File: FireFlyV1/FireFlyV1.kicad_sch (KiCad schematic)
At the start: 28 parts, among them SW1 PTS810SJG250SMTRLFS, U1 RP2040, U2 W25Q32JVSS, U3 ABM8-272-T3_C20625731, U4 NCP1117ST33T3G, U5 MCP6001T-I/OT

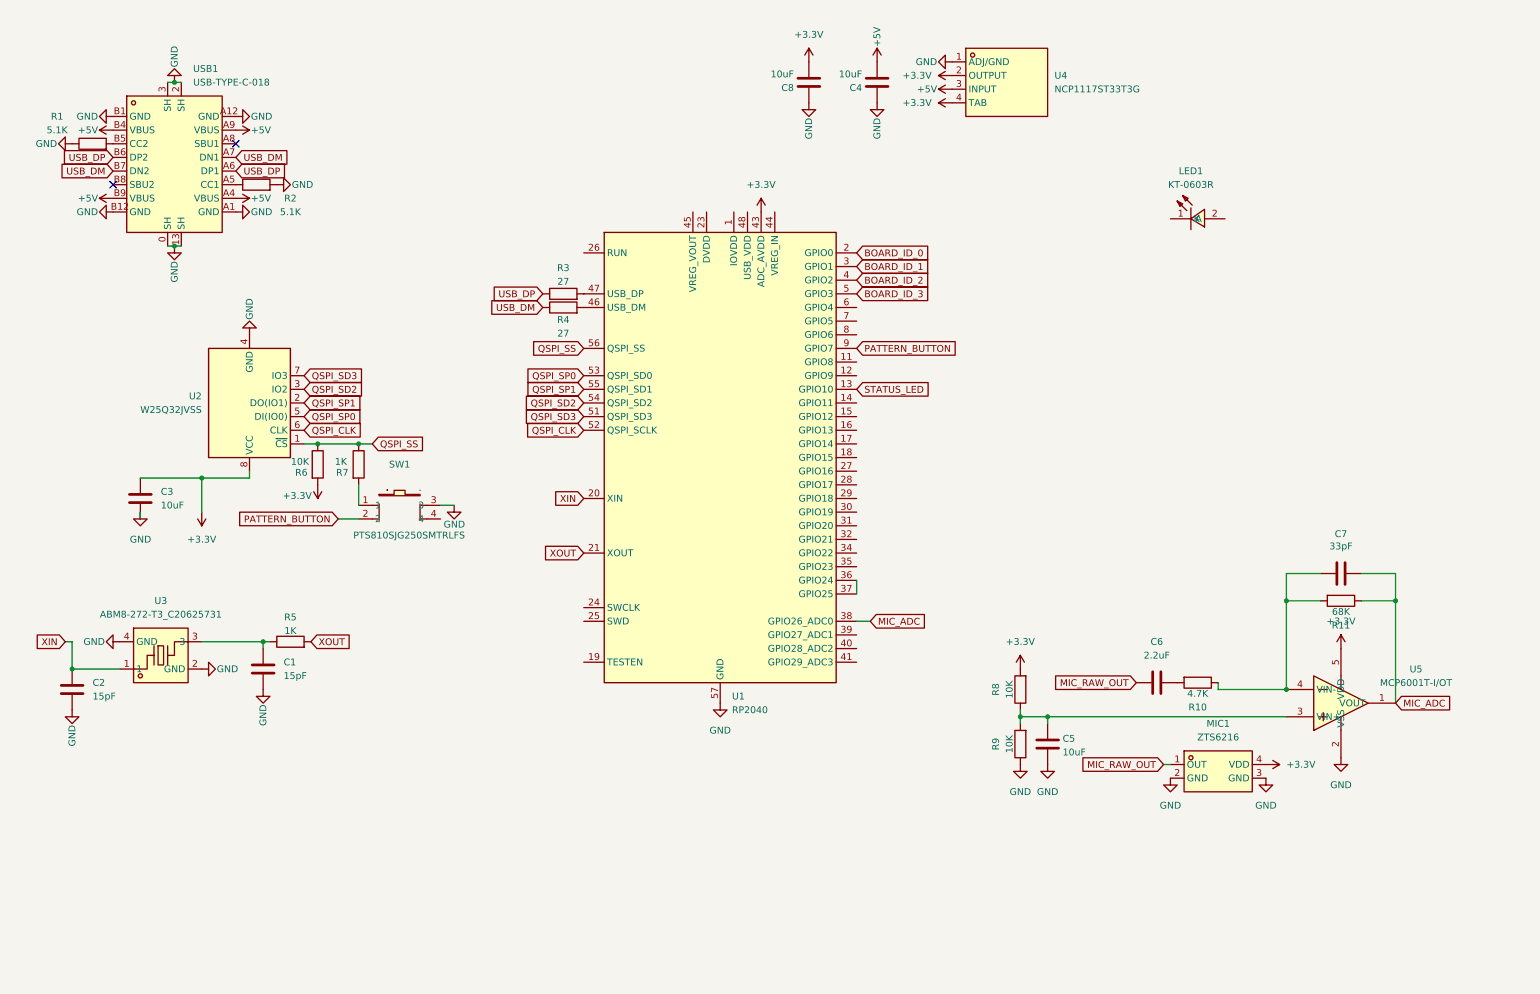
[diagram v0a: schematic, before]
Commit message: finished first draft of schematic
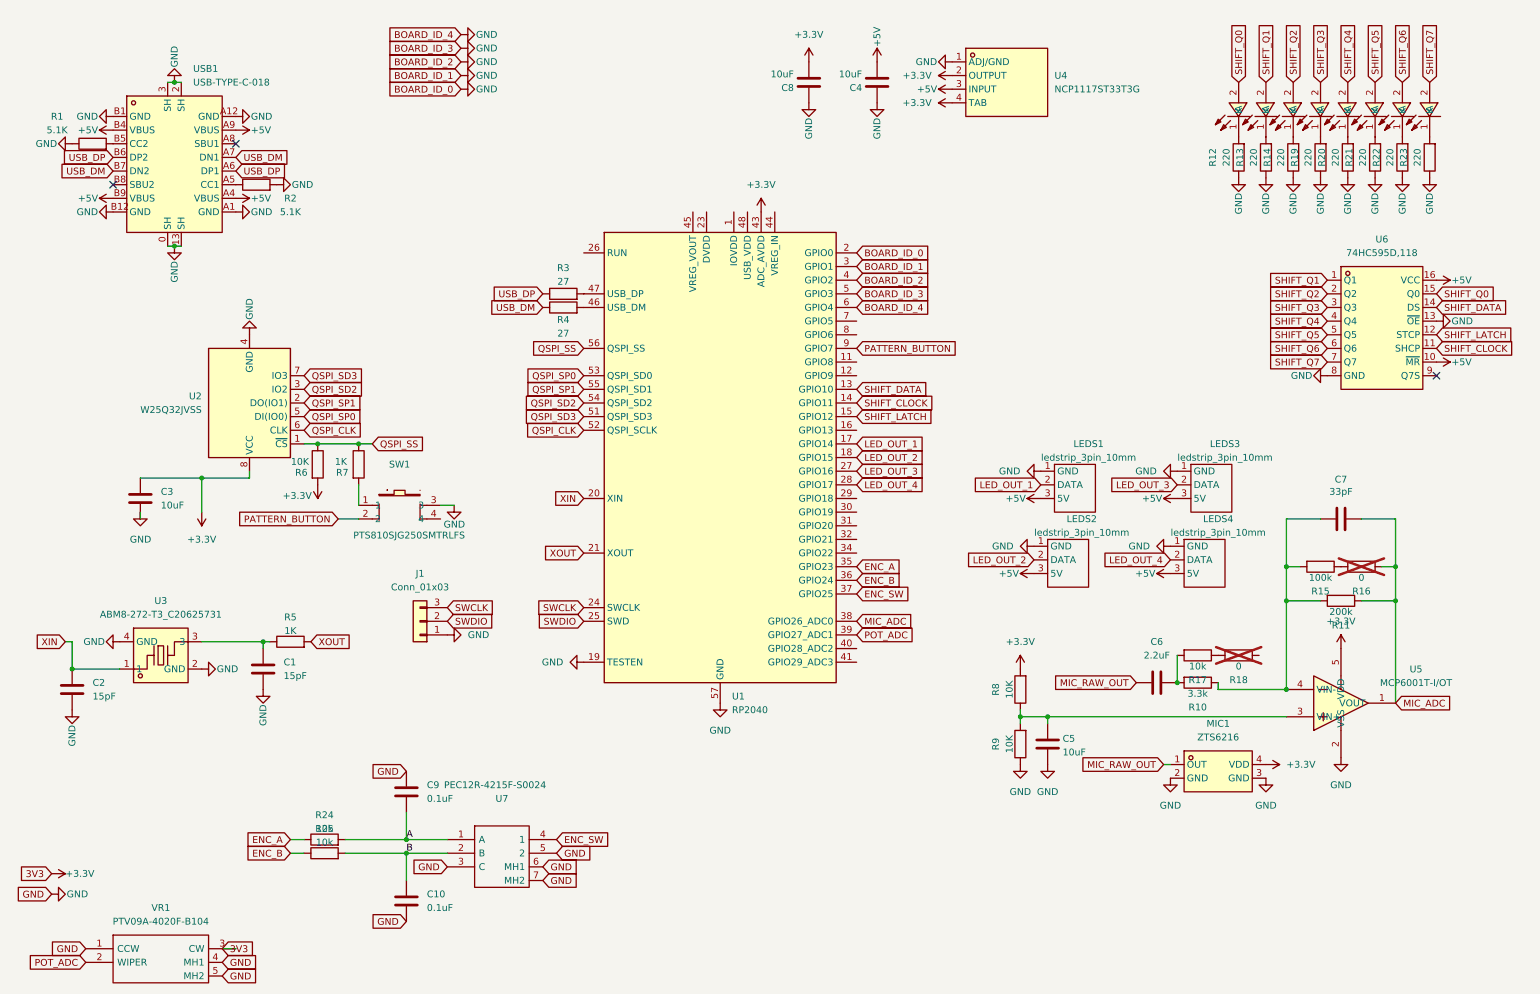
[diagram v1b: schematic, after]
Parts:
- added C10, C9: 0.1uF, symbol Device:C
- added J1: Conn_01x03, symbol Connector_Generic:Conn_01x03
- added LED2, LED3, LED4, LED5, LED6, LED7, LED8: KT-0603R, easyeda2kicad:LED0603-RD, symbol easyeda2kicad:KT-0603R
- added LEDS1, LEDS2, LEDS3, LEDS4: ledstrip_3pin_10mm, kylarLEDs:ledstrip_3pin_10mm, symbol kylarLEDs:ledstrip_3pin_10mm
- added R12, R13, R14, R19, R20, R21, R22, R23: 220, Resistor_SMD:R_0402_1005Metric, symbol Device:R
- added R15: 100k, Resistor_SMD:R_0402_1005Metric, symbol Device:R
- added R16, R18: 0, Resistor_SMD:R_0402_1005Metric, symbol Device:R
- added R17, R24, R25: 10k, Resistor_SMD:R_0402_1005Metric, symbol Device:R
- added U6: 74HC595D,118, easyeda2kicad:SOIC-16_L9.9-W3.9-P1.27-LS6.0-BL, symbol easyeda2kicad:74HC595D,118
- added U7: PEC12R-4215F-S0024, SamacSys_Parts:PEC12R-4XXXF-SXXXX_court, symbol SamacSys_Parts:PEC12R-4215F-S0024
- added VR1: PTV09A-4020F-B104, SamacSys_Parts:PTV09A4020FB103, symbol SamacSys_Parts:PTV09A-4020F-B104
- R1, R2, R3, R4, R5, R6, R7, R8, R9: footprint (none) -> Resistor_SMD:R_0402_1005Metric
- R10: value 4.7K -> 3.3k; footprint (none) -> Resistor_SMD:R_0402_1005Metric
- R11: value 68K -> 200k; footprint (none) -> Resistor_SMD:R_0402_1005Metric
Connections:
- net BOARD_ID_0 is gone; now on net GND: U1.2 (GPIO0)
- net BOARD_ID_1 is gone; now on net GND: U1.3 (GPIO1)
- net BOARD_ID_2 is gone; now on net GND: U1.4 (GPIO2)
- net BOARD_ID_3 is gone; now on net GND: U1.5 (GPIO3)
- net +3.3V: now also VR1.3 (CW)
- net +5V: now also LEDS1.3 (5V), LEDS2.3 (5V), LEDS3.3 (5V), LEDS4.3 (5V), U6.10 (~{MR}), U6.16 (VCC)
- net GND: now also U1.19 (TESTEN), U1.6 (GPIO4), C10.1, C9.2, J1.1 (Pin_1), LEDS1.1 (GND), LEDS2.1 (GND), LEDS3.1 (GND), LEDS4.1 (GND), R12.1, R13.1, R14.1, R19.1, R20.1, R21.1, R22.1, R23.1, U6.13 (~{OE}), U6.8 (GND), U7.3 (C), U7.5 (2), U7.6 (MH1), U7.7 (MH2), VR1.1 (CCW), VR1.4 (MH1), VR1.5 (MH2)
- net MIC_ADC: now also R16.1
- net SHIFT_CLOCK: now reaches U1.14 (GPIO11)
- net SHIFT_CLOCK: now also U6.11 (SHCP)
- net SHIFT_LATCH: now reaches U1.15 (GPIO12)
- net SHIFT_LATCH: now also U6.12 (STCP)
- net LED_OUT_1: now reaches U1.17 (GPIO14)
- net LED_OUT_1: now also LEDS1.2 (DATA)
- net LED_OUT_2: now reaches U1.18 (GPIO15)
- net LED_OUT_2: now also LEDS2.2 (DATA)
- net SWCLK: now reaches U1.24 (SWCLK)
- net SWCLK: now also J1.3 (Pin_3)
- net SWDIO: now reaches U1.25 (SWD)
- net SWDIO: now also J1.2 (Pin_2)
- net LED_OUT_3: now reaches U1.27 (GPIO16)
- net LED_OUT_3: now also LEDS3.2 (DATA)
- net LED_OUT_4: now reaches U1.28 (GPIO17)
- net LED_OUT_4: now also LEDS4.2 (DATA)
- net ENC_A: now reaches U1.35 (GPIO23)
- net ENC_A: now also R24.1
- net ENC_B: now reaches U1.36 (GPIO24)
- net ENC_B: now also R25.1; no longer U1.37 (GPIO25)
- net POT_ADC: now reaches U1.39 (GPIO27_ADC1)
- net POT_ADC: now also VR1.2 (WIPER)
- net at LED1.1 (K): now also R12.2
- net SHIFT_Q0: now reaches LED1.2 (A)
- net SHIFT_Q0: now also U6.15 (Q0)
- net at C7.1, R10.1, R11.2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: now also R15.2
- net at C6.2, R10.2: now also R17.2
- net STATUS_LED renamed SHIFT_DATA
- net SHIFT_DATA: now also U6.14 (DS)
- new net: LED2.1 (K), R13.2
- new net: LED8.1 (K), R23.2
- new net: R17.1, R18.2
- new net: R15.1, R16.2
- new net: LED6.1 (K), R21.2
- new net: LED3.1 (K), R14.2
- new net: LED4.1 (K), R19.2
- new net: LED5.1 (K), R20.2
- new net: LED7.1 (K), R22.2
- new net A: C9.1, R24.2, U7.1 (A)
- new net B: C10.2, R25.2, U7.2 (B)
- new net ENC_SW: U1.37 (GPIO25), U7.4 (1)
- new net SHIFT_Q1: LED2.2 (A), U6.1 (Q1)
- new net SHIFT_Q2: LED3.2 (A), U6.2 (Q2)
- new net SHIFT_Q3: LED4.2 (A), U6.3 (Q3)
- new net SHIFT_Q4: LED5.2 (A), U6.4 (Q4)
- new net SHIFT_Q5: LED6.2 (A), U6.5 (Q5)
- new net SHIFT_Q6: LED7.2 (A), U6.6 (Q6)
- new net SHIFT_Q7: LED8.2 (A), U6.7 (Q7)
- no-connect marks 2 -> 3
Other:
- moved on the sheet: C7

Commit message: lower cost regulator and crystal
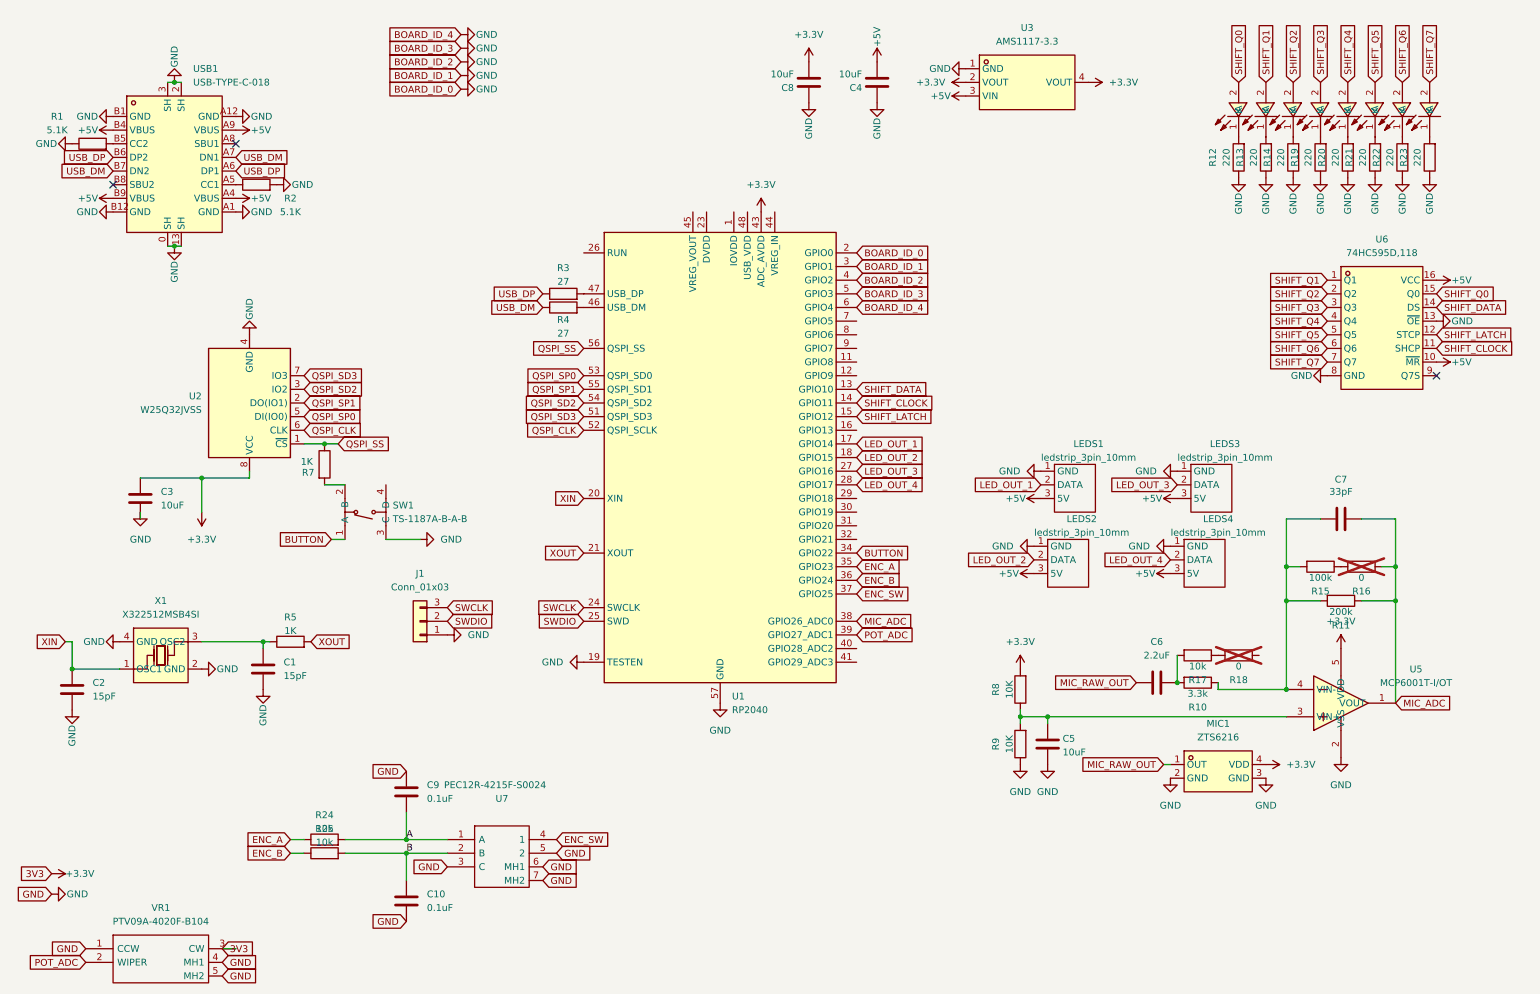
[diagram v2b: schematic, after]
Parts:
- removed R6: 10K, Resistor_SMD:R_0402_1005Metric, symbol Device:R
- removed SW1: PTS810SJG250SMTRLFS, easyeda2kicad:SW-SMD_4P_PTS810SJM250SMTRLFS, symbol easyeda2kicad:PTS810SJG250SMTRLFS
- removed U3: ABM8-272-T3_C20625731, easyeda2kicad:CRYSTAL-SMD_4P-L3.2-W2.5-BL, symbol easyeda2kicad:ABM8-272-T3_C20625731
- removed U4: NCP1117ST33T3G, easyeda2kicad:SOT-223-3_L6.5-W3.4-P2.30-LS7.0-BR, symbol easyeda2kicad:NCP1117ST33T3G
- added SW1: TS-1187A-B-A-B, easyeda2kicad:SW-SMD_4P-L5.1-W5.1-P3.70-LS6.5-TL-2, symbol easyeda2kicad:TS-1187A-B-A-B
- added U3: AMS1117-3.3, easyeda2kicad:SOT-223-3_L6.5-W3.4-P2.30-LS7.0-BR, symbol easyeda2kicad:AMS1117-3.3
- added X1: X322512MSB4SI, easyeda2kicad:OSC-SMD_4P-L3.2-W2.5-BL, symbol easyeda2kicad:X322512MSB4SI
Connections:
- net +3.3V: now also U3.2 (VOUT), U3.4 (VOUT)
- net +5V: now also U3.3 (VIN)
- net GND: now also SW1.3 (C), U3.1 (GND), X1.2 (GND), X1.4 (GND)
- net XIN: now also X1.1 (OSC1)
- net at C1.2, R5.1: now also X1.3 (OSC2)
- net BUTTON: now reaches U1.34 (GPIO22)
- net BUTTON: now also SW1.1 (A)
- net at R7.2: now also SW1.2 (B)
- net PATTERN_BUTTON: no longer names the net of U1.9 (GPIO7)
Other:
- moved on the sheet: R7

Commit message: FireFlyV1 power pins
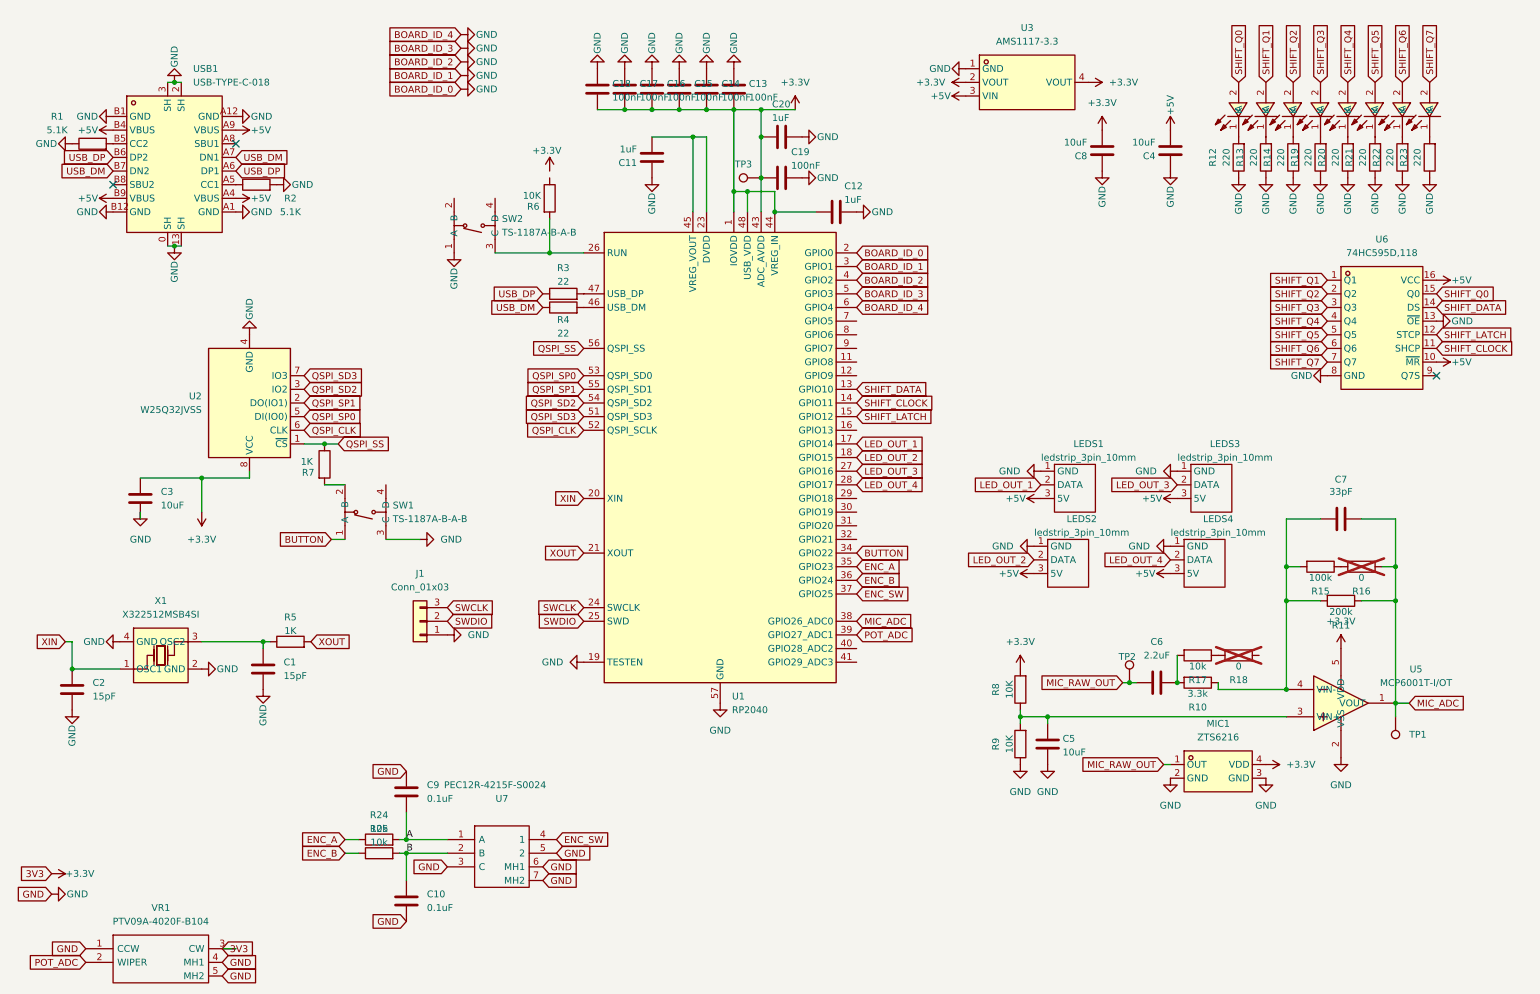
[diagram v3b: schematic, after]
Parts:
- added C11, C12, C20: 1uF, Capacitor_SMD:C_0402_1005Metric, symbol Device:C
- added C13, C14, C15, C16, C17, C18, C19: 100nF, Capacitor_SMD:C_0402_1005Metric, symbol Device:C
- added R6: 10K, Resistor_SMD:R_0402_1005Metric, symbol Device:R
- added SW2: TS-1187A-B-A-B, easyeda2kicad:SW-SMD_4P-L5.1-W5.1-P3.70-LS6.5-TL-2, symbol easyeda2kicad:TS-1187A-B-A-B
- added TP1, TP2, TP3: TestPoint, symbol Connector:TestPoint
- C1, C10, C2, C3, C4, C5, C6, C7, C8, C9: footprint (none) -> Capacitor_SMD:C_0402_1005Metric
- R3, R4: value 27 -> 22
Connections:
- net +3.3V: now also U1.1 (IOVDD), U1.10 (IOVDD), U1.22 (IOVDD), U1.33 (IOVDD), U1.42 (IOVDD), U1.44 (VREG_IN), U1.48 (USB_VDD), U1.49 (IOVDD), C12.1, C13.1, C14.1, C15.1, C16.1, C17.1, C18.1, C19.1, C20.1, TP3.1
- net GND: now also C11.2, C12.2, C13.2, C14.2, C15.2, C16.2, C17.2, C18.2, C19.2, C20.2, SW2.1 (A)
- net MIC_ADC: now also TP1.1
- net MIC_RAW_OUT: now also TP2.1
- net at U1.23 (DVDD), U1.50 (DVDD): now also U1.45 (VREG_VOUT), C11.1
- net at U1.26 (RUN): now also R6.2, SW2.3 (C)
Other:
- moved on the sheet: C4, C8, R24, R25

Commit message: FireFlyV1 PCB begin
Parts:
- removed TP3: TestPoint, symbol Connector:TestPoint
- added J2, J3, J4, J5: Conn_01x03, Connector_PinHeader_2.54mm:PinHeader_1x03_P2.54mm_Vertical, symbol Connector_Generic:Conn_01x03
- J1: footprint (none) -> Connector_PinHeader_2.54mm:PinHeader_1x03_P2.54mm_Vertical
- LEDS1, LEDS2, LEDS3, LEDS4: footprint kylarLEDs:ledstrip_3pin_10mm -> mouser:ledstrip_3pin_10mm
- TP1, TP2: footprint (none) -> TestPoint:TestPoint_Loop_D1.80mm_Drill1.0mm_Beaded
- U7: footprint SamacSys_Parts:PEC12R-4XXXF-SXXXX_court -> mouser:PEC12R-4XXXF-SXXXX_court
- VR1: footprint SamacSys_Parts:PTV09A4020FB103 -> mouser:PTV09A4020FB103
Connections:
- net +5V: now also J2.3 (Pin_3), J3.3 (Pin_3), J4.3 (Pin_3), J5.3 (Pin_3)
- net GND: now also J2.1 (Pin_1), J3.1 (Pin_1), J4.1 (Pin_1), J5.1 (Pin_1)
- net LED_OUT_1: now also J2.2 (Pin_2)
- net LED_OUT_2: now also J3.2 (Pin_2)
- net LED_OUT_3: now also J4.2 (Pin_2)
- net LED_OUT_4: now also J5.2 (Pin_2)
- no-connect marks 3 -> 13
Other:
- moved on the sheet: LEDS1, LEDS2, LEDS3, LEDS4, U6
